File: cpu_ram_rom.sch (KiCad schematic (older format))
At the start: 14 parts, among them U12 74HCT3G04, U4 Z84C0010AEG, U5 IS62C5128BL-45TLI, U6 SST39SF040

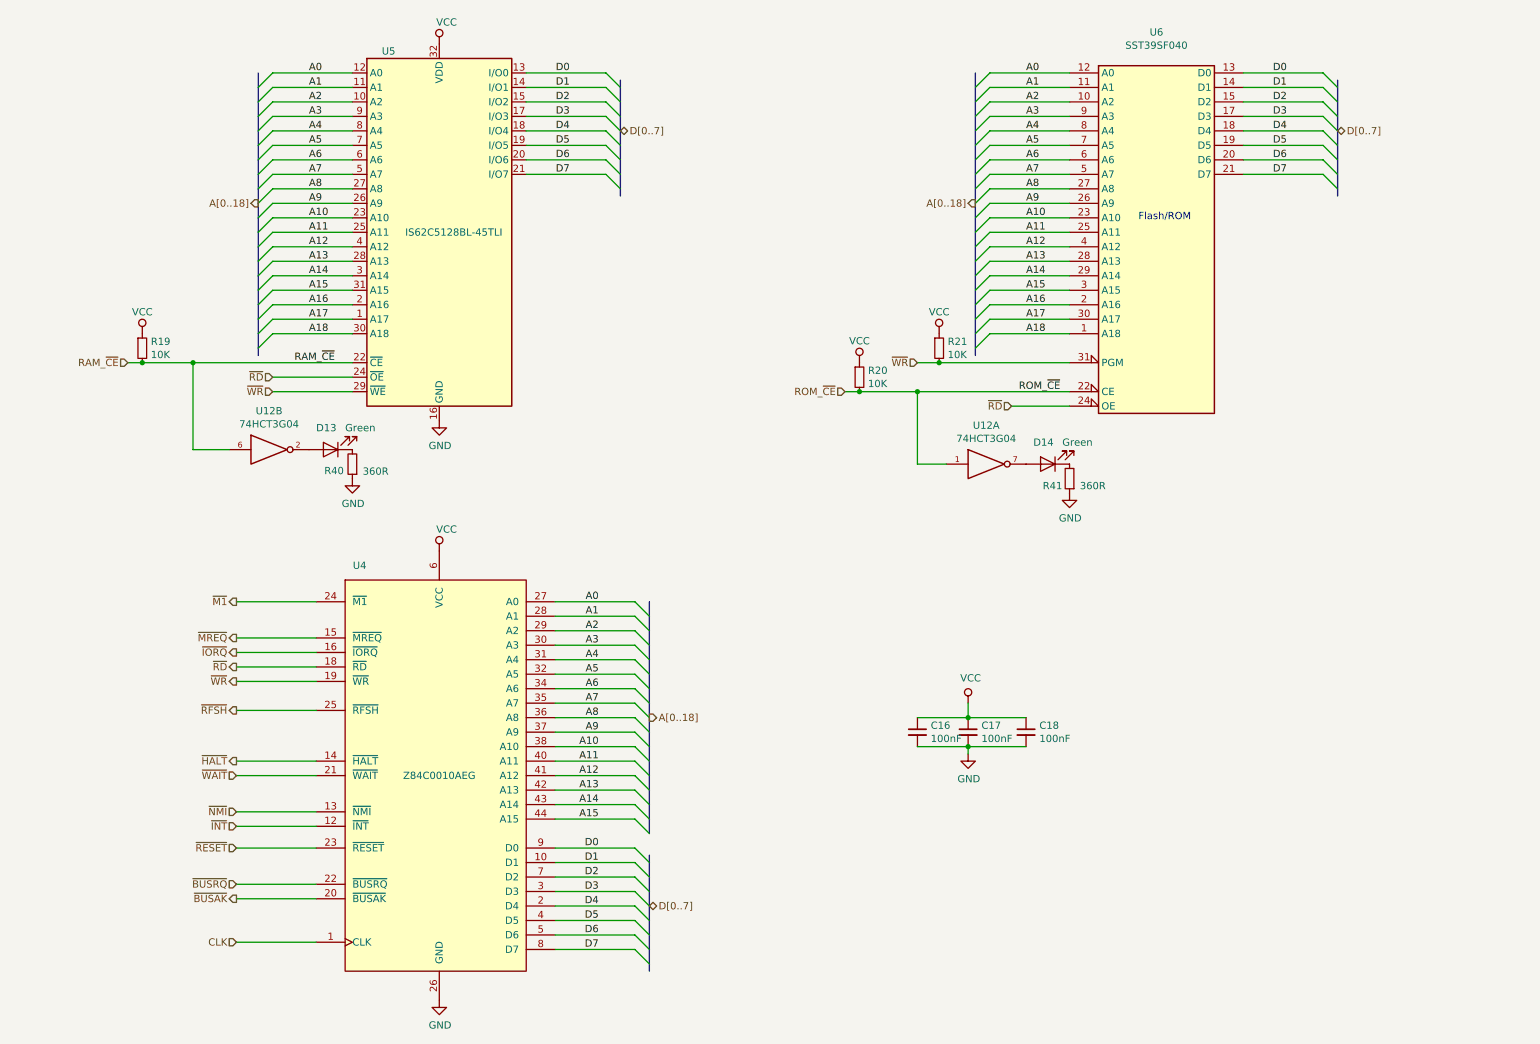
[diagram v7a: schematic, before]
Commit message: replaced VCC with 5V, fixed ROM footprint
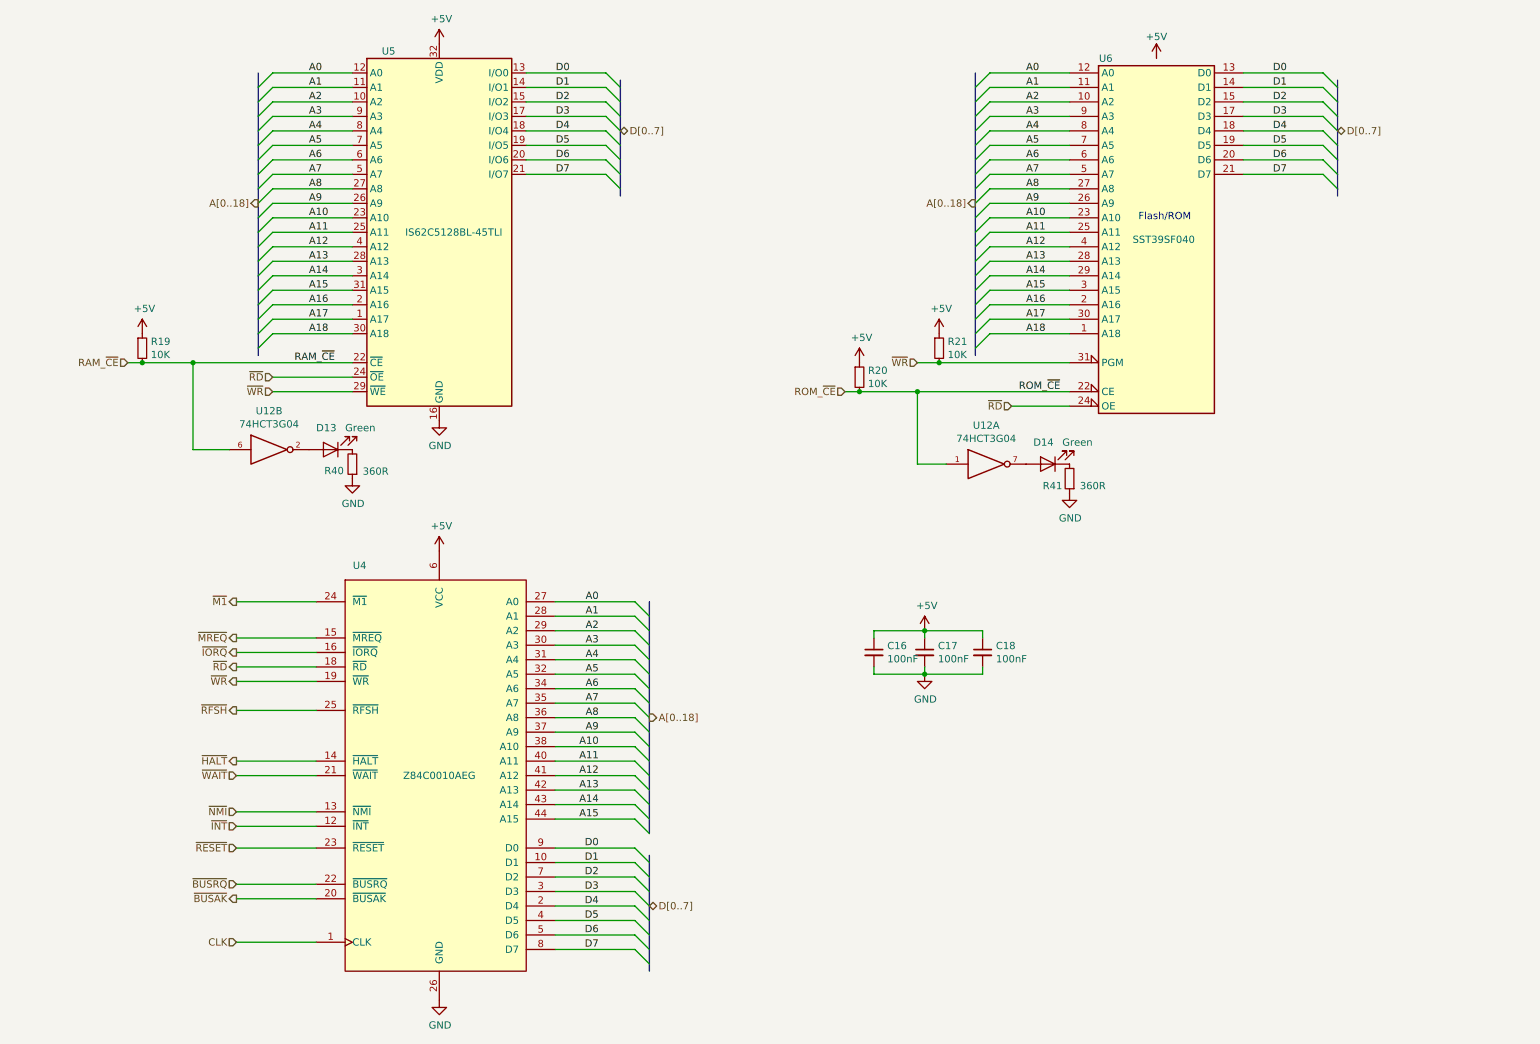
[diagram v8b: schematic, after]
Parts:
- U6: footprint Package_LCC:PLCC-32_SMD-Socket -> Package_LCC:PLCC-32_11.4x14.0mm_P1.27mm
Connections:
- net VCC renamed +5V
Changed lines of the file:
@@
 ~WR
-$Comp
-L power:VCC #PWR048
-U 1 1 5D8A4BED
-P 3650 800
-F 0 "#PWR048" H 3650 650 50  0001 C CNN
-F 1 "VCC" H 3700 950 50  0000 C CNN
-F 2 "" H 3650 800 50  0001 C CNN
-F 3 "" H 3650 800 50  0001 C CNN
-	1    3650 800
-	1    0    0    -1
-$EndComp
 $Comp
 L power:GND #PWR?
@@
 F 7 "Z84C0010AEG" H 950 7150 50  0001 L CNN "Manufacturer_Part_Number"
 	1    3650 5850
-	1    0    0    -1
-$EndComp
-$Comp
-L power:VCC #PWR044
-U 1 1 5F335870
-P 3650 4300
-F 0 "#PWR044" H 3650 4150 50  0001 C CNN
-F 1 "VCC" H 3700 4450 50  0000 C CNN
-F 2 "" H 3650 4300 50  0001 C CNN
-F 3 "" H 3650 4300 50  0001 C CNN
-	1    3650 4300
 	1    0    0    -1
 $EndComp
@@
 D[0..7]
 $Comp
-L Device:C_Small C?
-U 1 1 5FC53517
-P 6950 5550
-AR Path="/5D70CA34/5FC53517" Ref="C?"  Part="1"
-AR Path="/5D6224DC/5FC53517" Ref="C16"  Part="1"
-F 0 "C16" H 7042 5596 50  0000 L CNN
-F 1 "100nF" H 7042 5505 50  0000 L CNN
-F 2 "Capacitor_SMD:C_0603_1608Metric_Pad1.05x0.95mm_HandSolder" H 6950 5550 50  0001 C CNN
-F 3 "~" H 6950 5550 50  0001 C CNN
-	1    6950 5550
-	1    0    0    -1
-$EndComp
-$Comp
-L Device:C_Small C?
-U 1 1 5FC5351D
-P 7300 5550
-AR Path="/5D70CA34/5FC5351D" Ref="C?"  Part="1"
-AR Path="/5D6224DC/5FC5351D" Ref="C17"  Part="1"
-F 0 "C17" H 7392 5596 50  0000 L CNN
-F 1 "100nF" H 7392 5505 50  0000 L CNN
-F 2 "Capacitor_SMD:C_0603_1608Metric_Pad1.05x0.95mm_HandSolder" H 7300 5550 50  0001 C CNN
-F 3 "~" H 7300 5550 50  0001 C CNN
-	1    7300 5550
-	1    0    0    -1
-$EndComp
-$Comp
-L Device:C_Small C?
-U 1 1 5FC53523
-P 7700 5550
-AR Path="/5D70CA34/5FC53523" Ref="C?"  Part="1"
-AR Path="/5D6224DC/5FC53523" Ref="C18"  Part="1"
-F 0 "C18" H 7792 5596 50  0000 L CNN
-F 1 "100nF" H 7792 5505 50  0000 L CNN
-F 2 "Capacitor_SMD:C_0603_1608Metric_Pad1.05x0.95mm_HandSolder" H 7700 5550 50  0001 C CNN
-F 3 "~" H 7700 5550 50  0001 C CNN
-	1    7700 5550
-	1    0    0    -1
-$EndComp
-Wire Wire Line
-	6950 5450 7300 5450
-Connection ~ 7300 5450
-Wire Wire Line
-	7300 5450 7700 5450
-Connection ~ 7300 5650
-Wire Wire Line
-	7300 5650 6950 5650
-Wire Wire Line
-	7700 5650 7300 5650
-$Comp
-L power:VCC #PWR?
-U 1 1 5FC5355B
-P 7300 5350
-AR Path="/5FC5355B" Ref="#PWR?"  Part="1"
-AR Path="/5D70CA34/5FC5355B" Ref="#PWR?"  Part="1"
-AR Path="/5D6224DC/5FC5355B" Ref="#PWR046"  Part="1"
-F 0 "#PWR046" H 7300 5200 50  0001 C CNN
-F 1 "VCC" H 7317 5523 50  0000 C CNN
-F 2 "" H 7300 5350 50  0001 C CNN
-F 3 "" H 7300 5350 50  0001 C CNN
-	1    7300 5350
-	1    0    0    -1
-$EndComp
-Wire Wire Line
-	7300 5450 7300 5350
-$Comp
 L power:GND #PWR?
 U 1 1 5FC53564
-P 7300 5700
+P 7000 5150
 AR Path="/5D70CA34/5FC53564" Ref="#PWR?"  Part="1"
 AR Path="/5D6224DC/5FC53564" Ref="#PWR047"  Part="1"
-F 0 "#PWR047" H 7300 5450 50  0001 C CNN
-F 1 "GND" H 7305 5527 50  0000 C CNN
-F 2 "" H 7300 5700 50  0001 C CNN
-F 3 "" H 7300 5700 50  0001 C CNN
-	1    7300 5700
-	1    0    0    -1
-$EndComp
-Wire Wire Line
-	7300 5700 7300 5650
+F 0 "#PWR047" H 7000 4900 50  0001 C CNN
+F 1 "GND" H 7005 4977 50  0000 C CNN
+F 2 "" H 7000 5150 50  0001 C CNN
+F 3 "" H 7000 5150 50  0001 C CNN
+	1    7000 5150
+	1    0    0    -1
+$EndComp
 $Comp
 L power:GND #PWR?
@@
 $EndComp
 $Comp
-L power:VCC #PWR042
-U 1 1 5D95955B
-P 6550 3000
-F 0 "#PWR042" H 6550 2850 50  0001 C CNN
-F 1 "VCC" H 6550 3150 50  0000 C CNN
-F 2 "" H 6550 3000 50  0001 C CNN
-F 3 "" H 6550 3000 50  0001 C CNN
-	1    6550 3000
-	1    0    0    -1
-$EndComp
-$Comp
 L Device:R_Small R19
 U 1 1 5D966170
@@
 F 3 "~" H 1600 2900 50  0001 C CNN
 	1    1600 2900
-	1    0    0    -1
-$EndComp
-$Comp
-L power:VCC #PWR041
-U 1 1 5D966176
-P 1600 2800
-F 0 "#PWR041" H 1600 2650 50  0001 C CNN
-F 1 "VCC" H 1600 2950 50  0000 C CNN
-F 2 "" H 1600 2800 50  0001 C CNN
-F 3 "" H 1600 2800 50  0001 C CNN
-	1    1600 2800
 	1    0    0    -1
 $EndComp
@@
 Flash/ROM
 $Comp
-L power:VCC #PWR050
-U 1 1 5D6533B2
-P 7100 2800
-F 0 "#PWR050" H 7100 2650 50  0001 C CNN
-F 1 "VCC" H 7100 2950 50  0000 C CNN
-F 2 "" H 7100 2800 50  0001 C CNN
-F 3 "" H 7100 2800 50  0001 C CNN
-	1    7100 2800
-	1    0    0    -1
-$EndComp
-$Comp
 L Memory_Flash:SST39SF040 U6
 U 1 1 5D653323
 P 8600 2200
-F 0 "U6" H 8600 3681 50  0000 C CNN
-F 1 "SST39SF040" H 8600 3590 50  0000 C CNN
-F 2 "Package_LCC:PLCC-32_SMD-Socket" H 8600 2500 50  0001 C CNN
+F 0 "U6" H 8250 3500 50  0000 C CNN
+F 1 "SST39SF040" H 8650 2250 50  0000 C CNN
+F 2 "Package_LCC:PLCC-32_11.4x14.0mm_P1.27mm" H 8600 2500 50  0001 C CNN
 F 3 "http://ww1.microchip.com/downloads/en/DeviceDoc/25022B.pdf" H 8600 2500 50  0001 C CNN
 	1    8600 2200
@@
 Wire Wire Line
 	6950 3200 6550 3200
+$Comp
+L power:+5V #PWR?
+U 1 1 5EE28A08
+P 1600 2800
+AR Path="/5D70CA34/5DC790D1/5EE28A08" Ref="#PWR?"  Part="1"
+AR Path="/5D6224DC/5EE28A08" Ref="#PWR0114"  Part="1"
+F 0 "#PWR0114" H 1600 2650 50  0001 C CNN
+F 1 "+5V" H 1615 2973 50  0000 C CNN
+F 2 "" H 1600 2800 50  0001 C CNN
+F 3 "" H 1600 2800 50  0001 C CNN
+	1    1600 2800
+	1    0    0    -1
+$EndComp
+$Comp
+L power:+5V #PWR?
+U 1 1 5EE3613C
+P 3650 800
+AR Path="/5D70CA34/5DC790D1/5EE3613C" Ref="#PWR?"  Part="1"
+AR Path="/5D6224DC/5EE3613C" Ref="#PWR0115"  Part="1"
+F 0 "#PWR0115" H 3650 650 50  0001 C CNN
+F 1 "+5V" H 3665 973 50  0000 C CNN
+F 2 "" H 3650 800 50  0001 C CNN
+F 3 "" H 3650 800 50  0001 C CNN
+	1    3650 800
+	1    0    0    -1
+$EndComp
+$Comp
+L power:+5V #PWR?
+U 1 1 5EE3CC00
+P 8600 900
+AR Path="/5D70CA34/5DC790D1/5EE3CC00" Ref="#PWR?"  Part="1"
+AR Path="/5D6224DC/5EE3CC00" Ref="#PWR0116"  Part="1"
+F 0 "#PWR0116" H 8600 750 50  0001 C CNN
+F 1 "+5V" H 8600 1050 50  0000 C CNN
+F 2 "" H 8600 900 50  0001 C CNN
+F 3 "" H 8600 900 50  0001 C CNN
+	1    8600 900
+	1    0    0    -1
+$EndComp
+$Comp
+L power:+5V #PWR?
+U 1 1 5EE4A222
+P 7100 2800
+AR Path="/5D70CA34/5DC790D1/5EE4A222" Ref="#PWR?"  Part="1"
+AR Path="/5D6224DC/5EE4A222" Ref="#PWR0117"  Part="1"
+F 0 "#PWR0117" H 7100 2650 50  0001 C CNN
+F 1 "+5V" H 7115 2973 50  0000 C CNN
+F 2 "" H 7100 2800 50  0001 C CNN
+F 3 "" H 7100 2800 50  0001 C CNN
+	1    7100 2800
+	1    0    0    -1
+$EndComp
+$Comp
+L power:+5V #PWR?
+U 1 1 5EE57410
+P 6550 3000
+AR Path="/5D70CA34/5DC790D1/5EE57410" Ref="#PWR?"  Part="1"
+AR Path="/5D6224DC/5EE57410" Ref="#PWR0118"  Part="1"
+F 0 "#PWR0118" H 6550 2850 50  0001 C CNN
+F 1 "+5V" H 6565 3173 50  0000 C CNN
+F 2 "" H 6550 3000 50  0001 C CNN
+F 3 "" H 6550 3000 50  0001 C CNN
+	1    6550 3000
+	1    0    0    -1
+$EndComp
+$Comp
+L power:+5V #PWR?
+U 1 1 5EE64806
+P 3650 4300
+AR Path="/5D70CA34/5DC790D1/5EE64806" Ref="#PWR?"  Part="1"
+AR Path="/5D6224DC/5EE64806" Ref="#PWR0119"  Part="1"
+F 0 "#PWR0119" H 3650 4150 50  0001 C CNN
+F 1 "+5V" H 3665 4473 50  0000 C CNN
+F 2 "" H 3650 4300 50  0001 C CNN
+F 3 "" H 3650 4300 50  0001 C CNN
+	1    3650 4300
+	1    0    0    -1
+$EndComp
+$Comp
+L power:+5V #PWR?
+U 1 1 5EE71A25
+P 7000 4850
+AR Path="/5D70CA34/5DC790D1/5EE71A25" Ref="#PWR?"  Part="1"
+AR Path="/5D6224DC/5EE71A25" Ref="#PWR0120"  Part="1"
+F 0 "#PWR0120" H 7000 4700 50  0001 C CNN
+F 1 "+5V" H 7015 5023 50  0000 C CNN
+F 2 "" H 7000 4850 50  0001 C CNN
+F 3 "" H 7000 4850 50  0001 C CNN
+	1    7000 4850
+	1    0    0    -1
+$EndComp
+$Comp
+L Device:C_Small C16
+U 1 1 5F181CA3
+P 6650 5000
+F 0 "C16" H 6742 5046 50  0000 L CNN
+F 1 "100nF" H 6742 4955 50  0000 L CNN
+F 2 "Capacitor_SMD:C_0603_1608Metric_Pad1.05x0.95mm_HandSolder" H 6650 5000 50  0001 C CNN
+F 3 "~" H 6650 5000 50  0001 C CNN
+	1    6650 5000
+	1    0    0    -1
+$EndComp
+$Comp
+L Device:C_Small C17
+U 1 1 5F182ACB
+P 7000 5000
+F 0 "C17" H 7092 5046 50  0000 L CNN
+F 1 "100nF" H 7092 4955 50  0000 L CNN
+F 2 "Capacitor_SMD:C_0603_1608Metric_Pad1.05x0.95mm_HandSolder" H 7000 5000 50  0001 C CNN
+F 3 "~" H 7000 5000 50  0001 C CNN
+	1    7000 5000
+	1    0    0    -1
+$EndComp
+$Comp
+L Device:C_Small C18
+U 1 1 5F189729
+P 7400 5000
+F 0 "C18" H 7492 5046 50  0000 L CNN
+F 1 "100nF" H 7492 4955 50  0000 L CNN
+F 2 "Capacitor_SMD:C_0603_1608Metric_Pad1.05x0.95mm_HandSolder" H 7400 5000 50  0001 C CNN
+F 3 "~" H 7400 5000 50  0001 C CNN
+	1    7400 5000
+	1    0    0    -1
+$EndComp
+Wire Wire Line
+	6650 4900 6650 4850
+Wire Wire Line
+	6650 4850 7000 4850
+Wire Wire Line
+	7400 4850 7400 4900
+Wire Wire Line
+	7000 4900 7000 4850
+Connection ~ 7000 4850
+Wire Wire Line
+	7000 4850 7400 4850
+Wire Wire Line
+	6650 5100 6650 5150
+Wire Wire Line
+	6650 5150 7000 5150
+Wire Wire Line
+	7400 5150 7400 5100
+Wire Wire Line
+	7000 5100 7000 5150
+Connection ~ 7000 5150
+Wire Wire Line
+	7000 5150 7400 5150
 Wire Bus Line
 	9850 1050 9850 1850
